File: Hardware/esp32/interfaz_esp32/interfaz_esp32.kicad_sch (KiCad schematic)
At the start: 32 parts, among them J1 Screw_Terminal_01x20, J10 Screw_Terminal_01x03, J11 Screw_Terminal_01x03, J12 Screw_Terminal_01x03, J13 Screw_Terminal_01x03, J14 Screw_Terminal_01x03, J15 Screw_Terminal_01x03, J16 Screw_Terminal_01x03, J17 Screw_Terminal_01x03, J18 Screw_Terminal_01x03, J19 Screw_Terminal_01x03, J2 Screw_Terminal_01x20, J20 Screw_Terminal_01x03, J21 Screw_Terminal_01x03, J22 Screw_Terminal_01x03, J23 Screw_Terminal_01x03, J24 Screw_Terminal_01x03, J25 Screw_Terminal_01x03, J26 Screw_Terminal_01x03, J27 Screw_Terminal_01x03, J28 Screw_Terminal_01x03, J29 Screw_Terminal_01x03, J3 Screw_Terminal_01x20, J30 Screw_Terminal_01x03, J31 Screw_Terminal_01x03, J32 Screw_Terminal_01x03, J4 Screw_Terminal_01x20, J5 Screw_Terminal_01x03, J6 Screw_Terminal_01x03, J7 Screw_Terminal_01x03, J8 Screw_Terminal_01x03, J9 Screw_Terminal_01x03

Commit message: Capacitores de desacople
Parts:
- added C1, C2: 100nF, Capacitor_THT:C_Disc_D4.3mm_W1.9mm_P5.00mm, symbol Device:C
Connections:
- net at J4.18 (Pin_18), J5.1 (Pin_1): now also C2.1
- net at J4.20 (Pin_20), J5.3 (Pin_3): now also C2.2
- net at J1.1 (Pin_1), J19.1 (Pin_1): now also C1.1
- net at J1.3 (Pin_3), J19.3 (Pin_3): now also C1.2
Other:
- moved on the sheet: J1, J10, J11, J12, J13, J14, J15, J16, J17, J18, J19, J2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

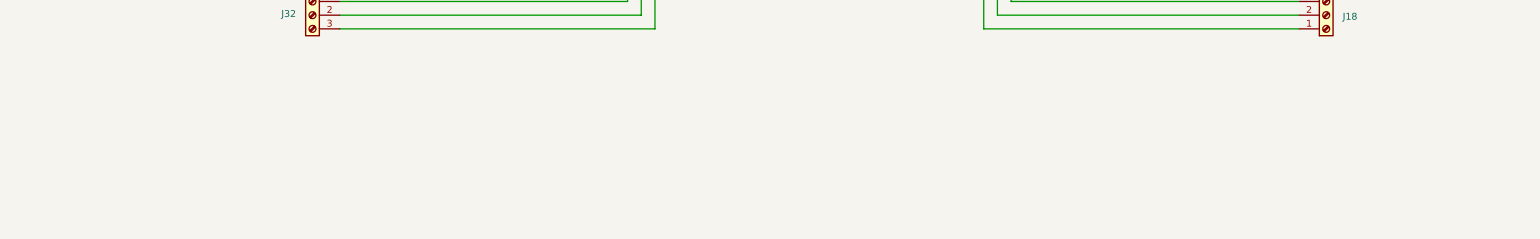
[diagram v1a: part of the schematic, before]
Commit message: Esquematicos de las PCB
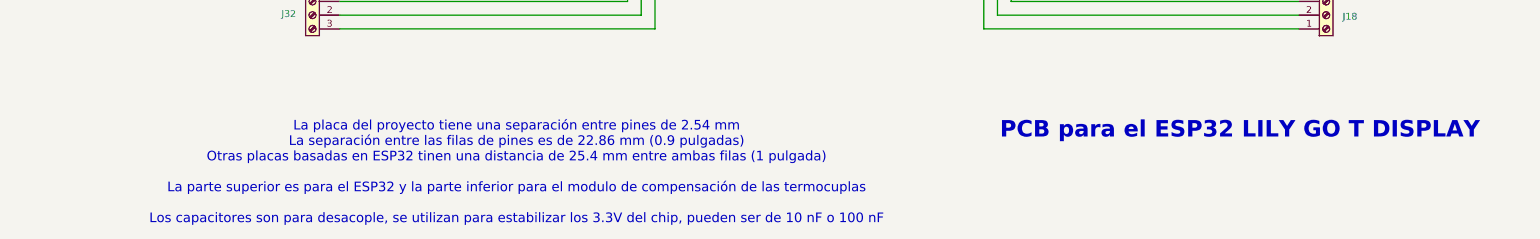
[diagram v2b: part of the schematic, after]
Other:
- note added: "La placa del proyecto tiene una separación entre pines de 2.54 mm La separación entre las filas de pines es de 22.86 mm (0.9 pulgadas) Otras placas basadas en ESP32 tinen una distancia de 25.4 mm entre ambas filas (1 pulgada) La parte superior es para el ESP32 y la parte inferior para el modulo de compensación de las termocuplas Los capacitores son para desacople, se utilizan para estabilizar los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"
- note added: "PCB para el ESP32 LILY GO T DISPLAY"
- company: (none) -> Digicontrol
- title: (none) -> PCB para el ESP32 LILY GO T DISPLAY
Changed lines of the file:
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@@
 	(generator_version "9.0")
 	(paper "A4")
+	(title_block
+		(title "PCB para el ESP32 LILY GO T DISPLAY")
+		(date "2025-10-04")
+		(company "Digicontrol")
+	)
+	(text "PCB para el ESP32 LILY GO T DISPLAY"
+		(exclude_from_sim no)
+		(at 227.838 173.736 0)
+		(effects
+			(font
+				(size 3.048 3.048)
+				(thickness 0.4064)
+				(bold yes)
+			)
+		)
+	)
+	(text "La placa del proyecto tiene una separación entre pines de 2.54 mm\nLa separación entre las filas de pines es de 22.86 mm (0.9 pulgadas)\nOtras placas basadas en ESP32 tinen una distancia de 25.4 mm entre ambas filas (1 pulgada)\n\nLa parte superior es para el ESP32 y la parte inferior para el modulo de compensación de las termocuplas\n\nLos capacitores son para desacople, se utilizan para estabilizar los 3.3V del chip, pueden ser de 10 nF o 100 nF\n"
+		(exclude_from_sim no)
+		(at 93.726 181.61 0)
+		(effects
+			(font
+				(size 1.778 1.778)
+			)
+		)
+	)
 	(junction
 		(at 105.41 39.37)
